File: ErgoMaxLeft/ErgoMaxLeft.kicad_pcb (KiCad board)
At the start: 2 copper layers, 182.8 x 178.9 mm, 97 parts, among them J1 AudioJack4_Ground, K1 KEYSW, K10 KEYSW, K11 KEYSW, K12 KEYSW, K13 KEYSW, K14 KEYSW, K15 KEYSW, K16 KEYSW, K17 KEYSW, K18 KEYSW, K19 KEYSW, K2 KEYSW, K20 KEYSW, K21 KEYSW, K22 KEYSW, K23 KEYSW, K24 KEYSW, K25 KEYSW, K26 KEYSW, K27 KEYSW, K28 KEYSW, K29 KEYSW, K3 KEYSW, K30 KEYSW, K31 KEYSW, K32 KEYSW, K33 KEYSW, K34 KEYSW, K35 KEYSW, K36 KEYSW, K37 KEYSW, K38 KEYSW, K39 KEYSW, K4 KEYSW, K40 KEYSW, K41 KEYSW, K42 KEYSW, K43 KEYSW, K44 KEYSW, K5 KEYSW, K6 KEYSW, K7 KEYSW, K8 KEYSW, K9 KEYSW, U1 ProMicro

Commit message: WIP PCB - add 2 zones and start routing
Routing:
- net /Row0: track 0.00 -> 110.6 mm
- added copper zone on B.Cu, net GND
- added copper zone on F.Cu, net GND
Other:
- net class Default: clearance 0.2 -> 0.3048; trace_width 0.25 -> 0.6; via_dia 0.8 -> 0.6096; via_drill 0.4 -> 0.508
- rule trace_clearance: 0.2 -> 0.3048
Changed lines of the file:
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@@
     (thickness 1.6)
     (drawings 13)
-    (tracks 0)
+    (tracks 24)
     (zones 0)
     (modules 97)
@@
   )
   (setup
-    (last_trace_width 0.25)
-    (trace_clearance 0.2)
+    (last_trace_width 0.6)
+    (trace_clearance 0.3048)
     (zone_clearance 0.508)
     (zone_45_only no)
@@
     (segment_width 0.381)
     (edge_width 0.381)
-    (via_size 0.8)
-    (via_drill 0.4)
+    (via_size 0.6096)
+    (via_drill 0.508)
     (via_min_size 0.4)
     (via_min_drill 0.3)
-    (uvia_size 0.3)
-    (uvia_drill 0.1)
+    (uvia_size 0.508)
+    (uvia_drill 0.127)
     (uvias_allowed no)
     (uvia_min_size 0.2)
@@
     (solder_mask_min_width 0.25)
     (aux_axis_origin 0 0)
-    (visible_elements 7FFFF7FF)
+    (visible_elements 7FFFFFFF)
     (pcbplotparams
       (layerselection 0x010fc_ffffffff)
@@
   (net 66 "Net-(U1-Pad24)")
   (net_class Default "Ceci est la Netclass par défaut."
-    (clearance 0.2)
-    (trace_width 0.25)
-    (via_dia 0.8)
-    (via_drill 0.4)
-    (uvia_dia 0.3)
-    (uvia_drill 0.1)
+    (clearance 0.3048)
+    (trace_width 0.6)
+    (via_dia 0.6096)
+    (via_drill 0.508)
+    (uvia_dia 0.508)
+    (uvia_drill 0.127)
     (add_net /Col0)
     (add_net /Col1)
@@
   (gr_line (start 119.865 168.575) (end 189.105 168.575) (layer Edge.Cuts) (width 0.381))
   (gr_line (start 110.34 29.315) (end 110.34 159.05) (layer Edge.Cuts) (width 0.381))
+  (segment (start 159.685 55.36704) (end 161.56 55.36704) (width 0.6) (layer F.Cu) (net 53))
+  (segment (start 143.8666 55.36704) (end 159.685 55.36704) (width 0.6) (layer F.Cu) (net 53))
+  (segment (start 142.51 56.72364) (end 143.8666 55.36704) (width 0.6) (layer F.Cu) (net 53))
+  (segment (start 142.51 58.57364) (end 142.51 56.72364) (width 0.6) (layer F.Cu) (net 53))
+  (segment (start 180.575 53.76964) (end 180.6 53.76964) (width 0.6) (layer F.Cu) (net 53))
+  (segment (start 178.725 51.91964) (end 180.575 53.76964) (width 0.6) (layer F.Cu) (net 53))
+  (segment (start 163.1574 51.91964) (end 178.725 51.91964) (width 0.6) (layer F.Cu) (net 53))
+  (segment (start 161.56 53.51704) (end 163.1574 51.91964) (width 0.6) (layer F.Cu) (net 53))
+  (segment (start 161.56 55.36704) (end 161.56 53.51704) (width 0.6) (layer F.Cu) (net 53))
+  (segment (start 197.765 55.35364) (end 199.64 55.35364) (width 0.6) (layer F.Cu) (net 53))
+  (segment (start 194.101199 51.689839) (end 197.765 55.35364) (width 0.6) (layer F.Cu) (net 53))
+  (segment (start 180.829801 51.689839) (end 194.101199 51.689839) (width 0.6) (layer F.Cu) (net 53))
+  (segment (start 180.6 51.91964) (end 180.829801 51.689839) (width 0.6) (layer F.Cu) (net 53))
+  (segment (start 180.6 53.76964) (end 180.6 51.91964) (width 0.6) (layer F.Cu) (net 53))
+  (segment (start 216.802751 56.65364) (end 218.677751 56.65364) (width 0.6) (layer F.Cu) (net 53))
+  (segment (start 213.42295 53.273839) (end 216.802751 56.65364) (width 0.6) (layer F.Cu) (net 53))
+  (segment (start 199.869801 53.273839) (end 213.42295 53.273839) (width 0.6) (layer F.Cu) (net 53))
+  (segment (start 199.64 53.50364) (end 199.869801 53.273839) (width 0.6) (layer F.Cu) (net 53))
+  (segment (start 199.64 55.35364) (end 199.64 53.50364) (width 0.6) (layer F.Cu) (net 53))
+  (segment (start 235.895 56.65564) (end 237.77 56.65564) (width 0.6) (layer F.Cu) (net 53))
+  (segment (start 233.813199 54.573839) (end 235.895 56.65564) (width 0.6) (layer F.Cu) (net 53))
+  (segment (start 218.907552 54.573839) (end 233.813199 54.573839) (width 0.6) (layer F.Cu) (net 53))
+  (segment (start 218.677751 54.80364) (end 218.907552 54.573839) (width 0.6) (layer F.Cu) (net 53))
+  (segment (start 218.677751 56.65364) (end 218.677751 54.80364) (width 0.6) (layer F.Cu) (net 53))
+  (zone (net 64) (net_name GND) (layer F.Cu) (hatch edge 0.508)
+    (connect_pads (clearance 0.508))
+    (min_thickness 0.254)
+    (fill yes (arc_segments 16) (thermal_gap 0.508) (thermal_bridge_width 0.508))
+    (polygon
+      (pts
+        (xy 113.5 26.16) (xy 250.48 26.15) (xy 253.64 29.32) (xy 253.66 137.28) (xy 258.5 137.32)
+        (xy 291.62 152.74) (xy 293.14 156.99) (xy 271.49 203.49) (xy 267.31 205.03) (xy 189.11 168.57)
+        (xy 119.88 168.55) (xy 110.3 159.03) (xy 110.33 29.34) (xy 113.5 26.17)
+      )
+    )
+  )
+  (zone (net 64) (net_name GND) (layer B.Cu) (hatch edge 0.508)
+    (connect_pads (clearance 0.508))
+    (min_thickness 0.254)
+    (fill yes (arc_segments 16) (thermal_gap 0.508) (thermal_bridge_width 0.508))
+    (polygon
+      (pts
+        (xy 113.5 26.16) (xy 250.48 26.15) (xy 253.64 29.32) (xy 253.66 137.28) (xy 258.5 137.32)
+        (xy 291.62 152.74) (xy 293.14 156.99) (xy 271.49 203.49) (xy 267.31 205.03) (xy 189.11 168.57)
+        (xy 119.88 168.55) (xy 110.3 159.03) (xy 110.33 29.34) (xy 113.5 26.17)
+      )
+    )
+  )
 )

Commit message: WIP PCB - more routing
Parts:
- moved D43 21.1 mm to (260.8, 168.8)
- moved D44 12.8 mm to (272.9, 185.8)
- moved D42 9.64 mm to (245.2, 169.8)
- moved D16 6.18 mm to (177.9, 98.6)
- moved D27 5.33 mm to (271.0, 159.1)
- moved D29 5.24 mm to (135.0, 144.4)
- moved D7 4.57 mm to (134.8, 87.3)
- moved D14 4.57 mm to (134.8, 106.3)
- moved D21 4.53 mm to (134.9, 125.3)
- moved D28 4.23 mm to (285.8, 167.2)
- moved D36 4.11 mm to (278.6, 183.4)
- moved D9 3.27 mm to (177.1, 83.9)
- moved D23 2.11 mm to (177.1, 121.7)
- moved D30 1.98 mm to (158.1, 144.1)
- moved D17 1.96 mm to (196.3, 101.3)
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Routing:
- net /Row3: track 0.00 -> 200.1 mm
- net /Col1: track 0.00 -> 191.1 mm
- net /Row4: track 0.00 -> 189.9 mm
- net /Row5: track 0.00 -> 163.5 mm
- net /Row2: track 0.00 -> 135.9 mm
- net /Row1: track 0.00 -> 135.0 mm
- net Net-(D1-Pad2): track 0.00 -> 4.31 mm

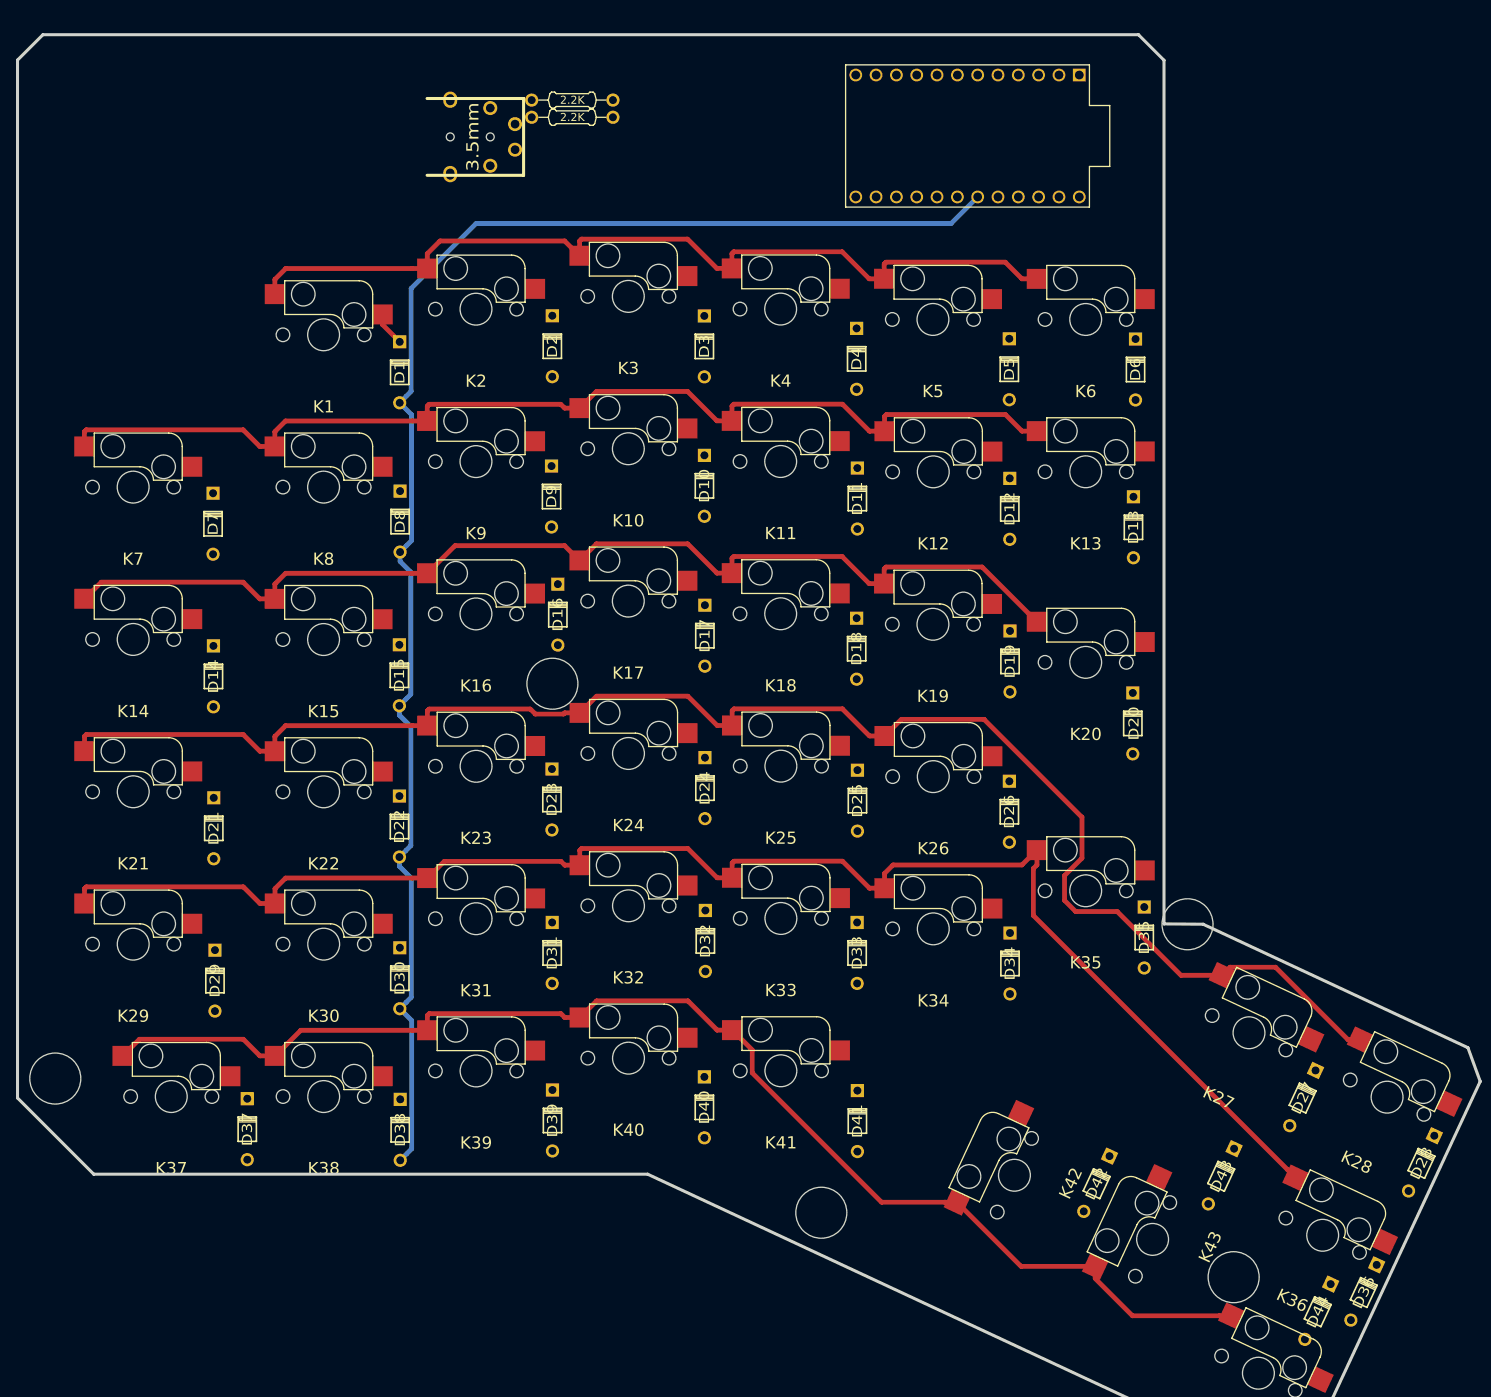
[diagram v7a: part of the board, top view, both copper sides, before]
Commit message: WIP PCB - update diodes footprints to something more accurate, displayed in the proper direction
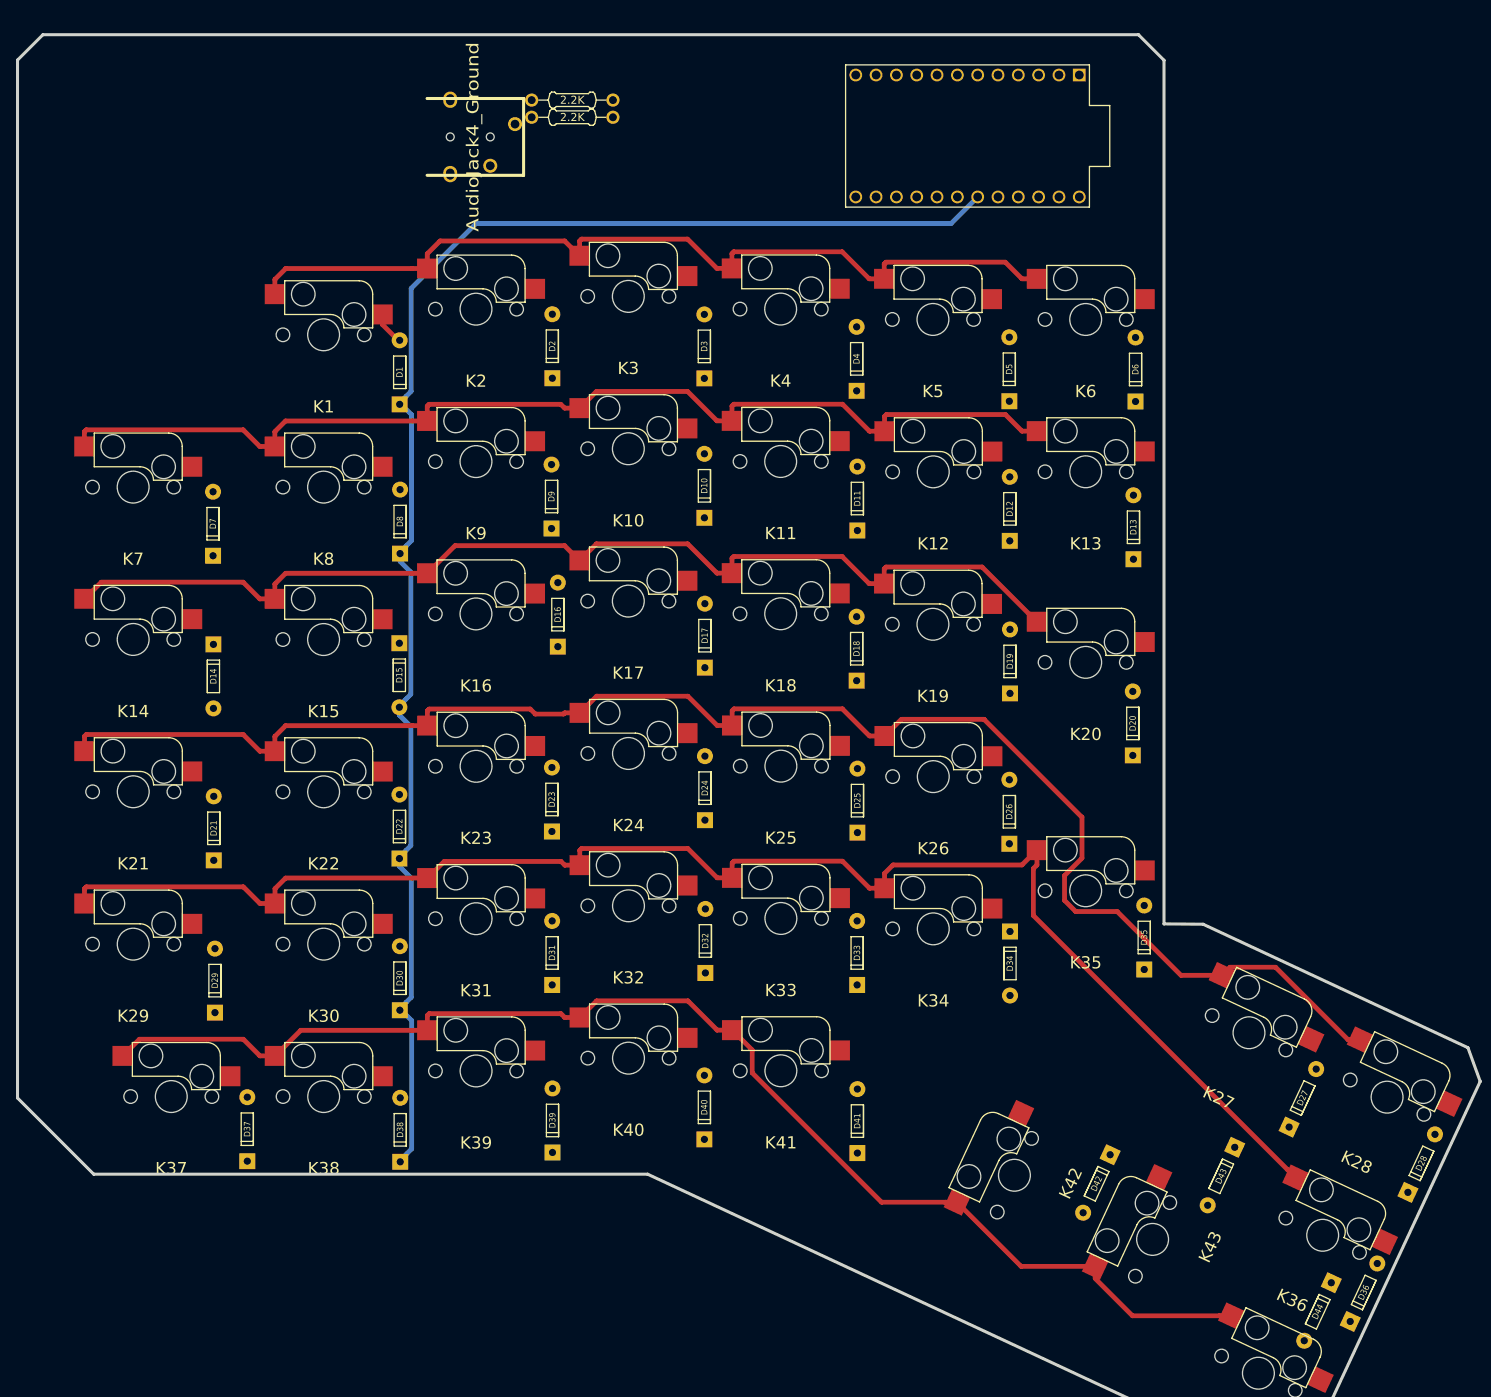
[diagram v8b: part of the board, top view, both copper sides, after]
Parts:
- removed ? (x4): , MountingHole:MountingHole_6.5mm_Pad
- removed ?: , MountingHole:MountingHole_6.4mm_M6
- D1, D10, D11, D12, D13, D14, D15, D16, D17, D18, D19, D2, D20, D21, D22, D23, D24, D25, D26, D27, D28, D29, D3, D30, D31, D32, D33, D34, D35, D36, D37, D38, D39, D4, D40, D41, D42, D43, D44, D5, D6, D7, D8, D9: footprint Keebio-Parts:Diode -> Keebio-Parts:Diode_Long
- J1: footprint Keebio-Parts:4pin35mmAudio -> keyboard_parts:4pin35mmAudio
- turned D1 to 270 degrees
- turned D10 to 270 degrees
- turned D11 to 270 degrees
- turned D12 to 270 degrees
- turned D13 to 270 degrees
- turned D16 to 270 degrees
- turned D17 to 270 degrees
- turned D18 to 270 degrees
- turned D19 to 270 degrees
- turned D2 to 270 degrees
- turned D20 to 270 degrees
- turned D21 to 270 degrees
- turned D22 to 270 degrees
- turned D23 to 270 degrees
- turned D24 to 270 degrees
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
